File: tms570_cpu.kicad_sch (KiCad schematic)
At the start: 49 parts, among them J12 TS-103-G-A, J2 FTSH-105-01-L-DV-K, U2 TMS570LS0914PGE

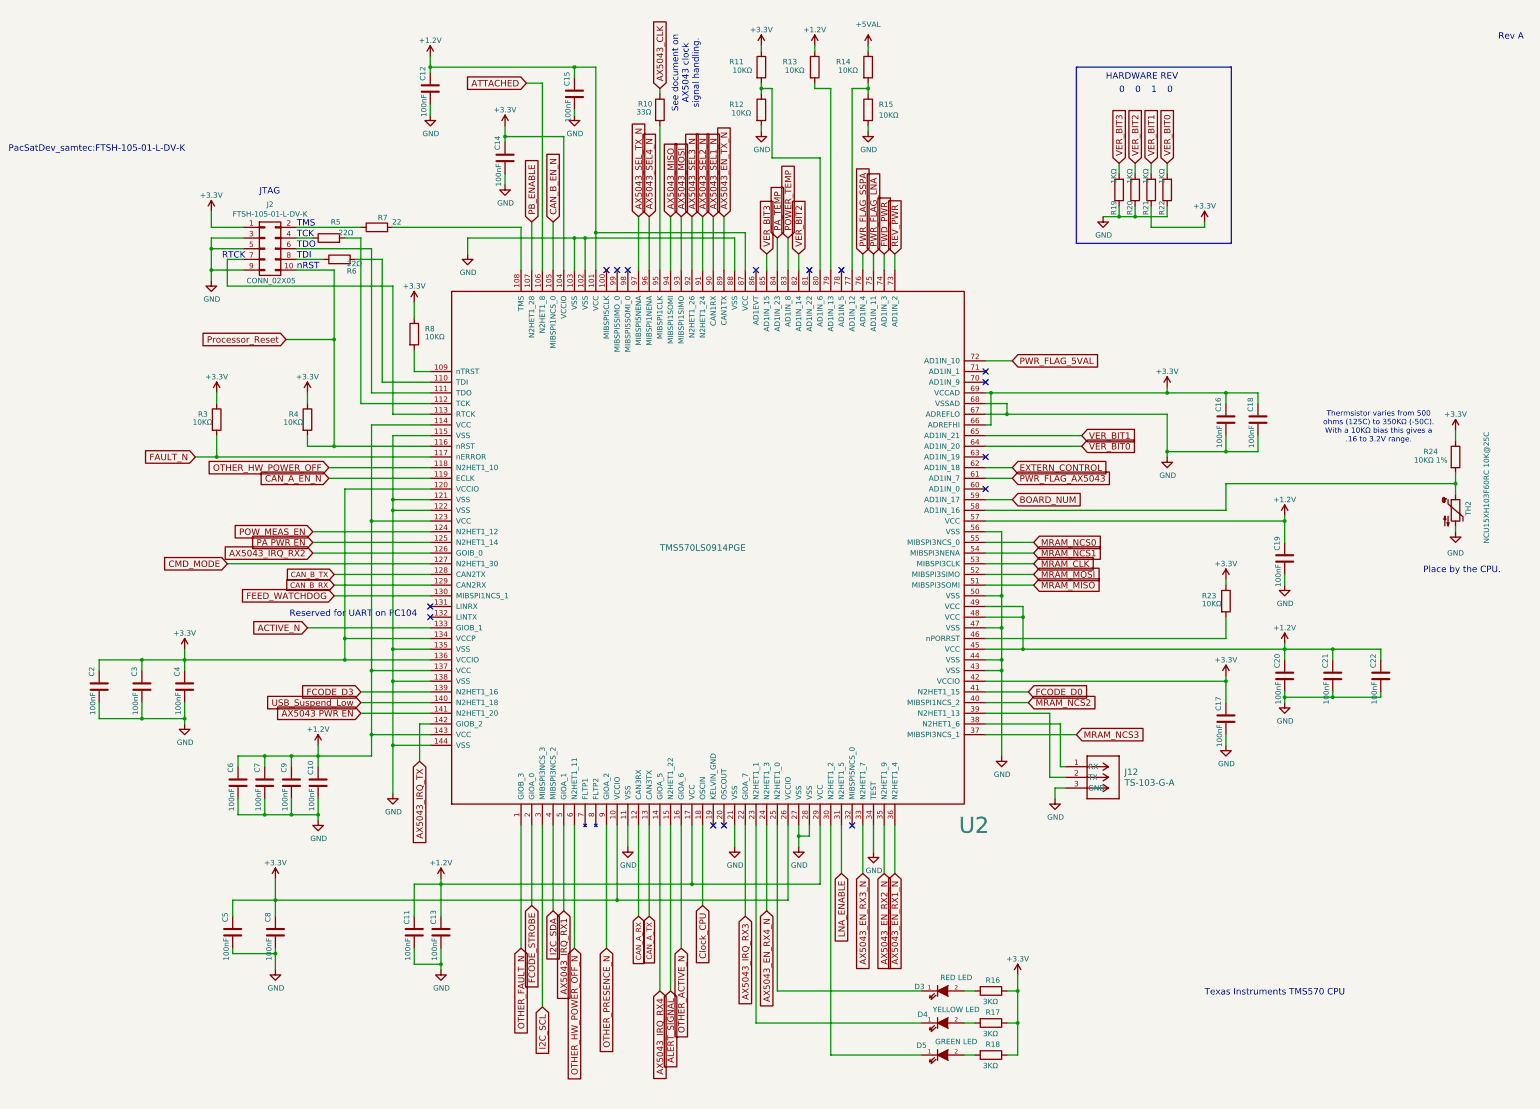
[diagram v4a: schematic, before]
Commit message: Finish up temporary PC104 assignments
Finish up most of what is required for the CubeSat Kit Bus conversion.

Signed-off-by: Corey Minyard <corey@minyard.net>
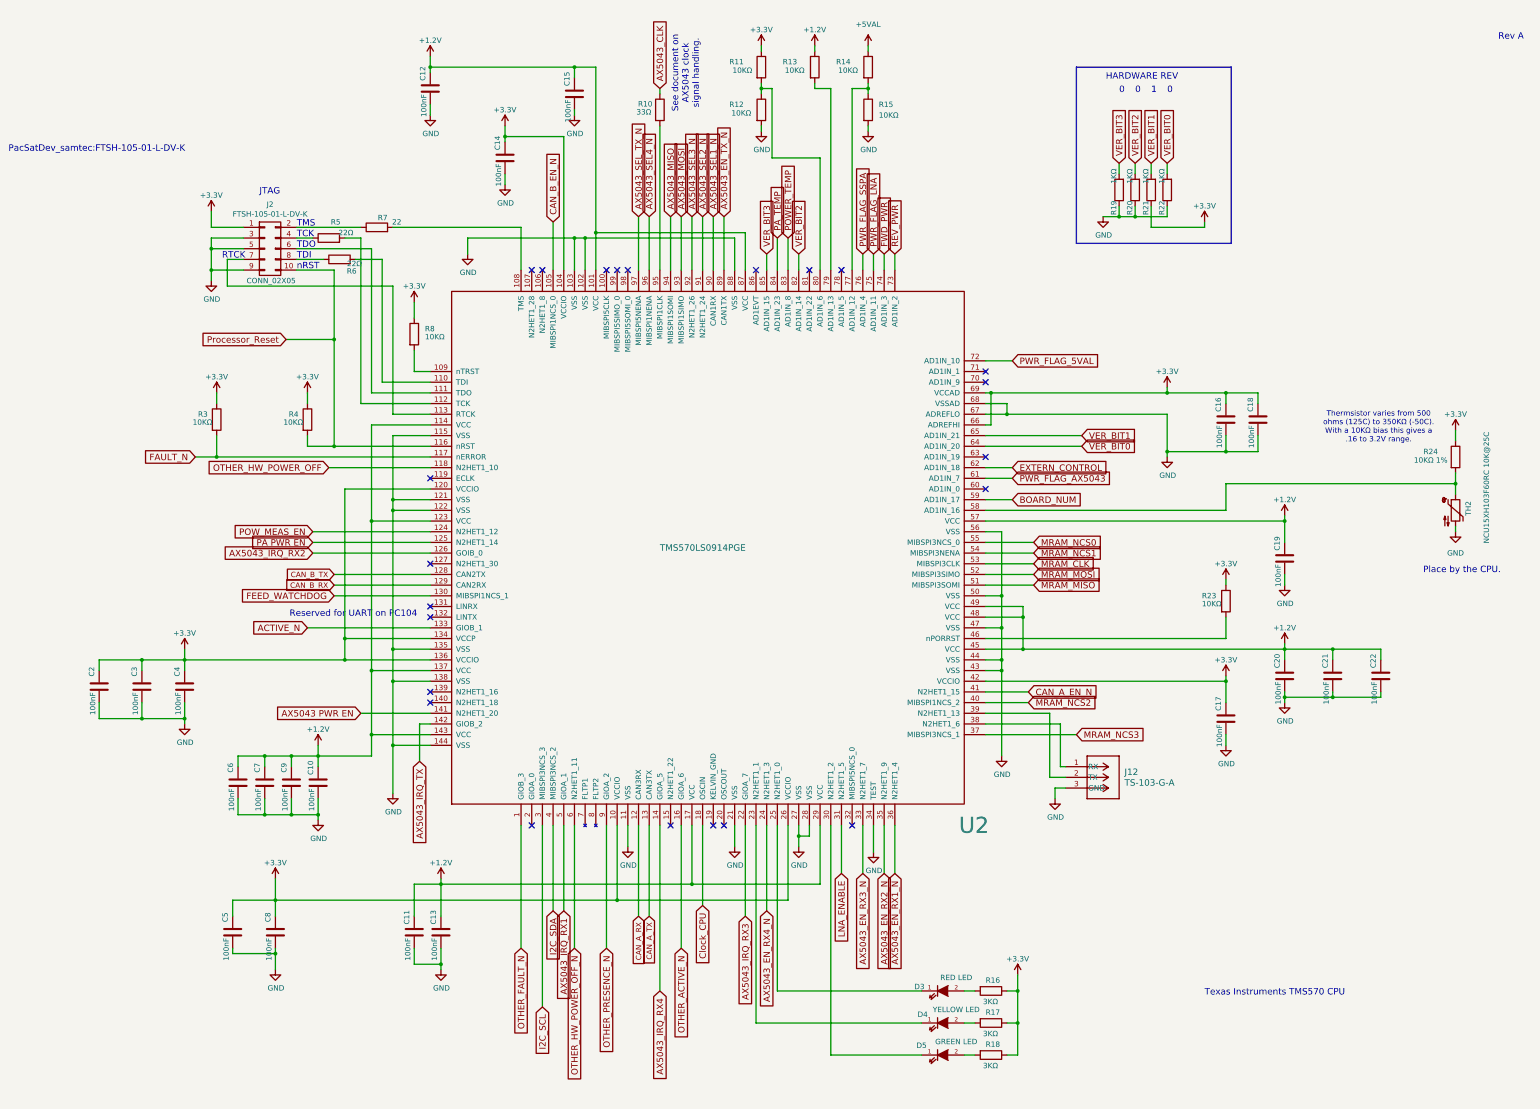
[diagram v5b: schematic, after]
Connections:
- net FCODE_D0 is gone; now on net CAN_A_EN_N: U2.41 (N2HET1_15)
- net CAN_A_EN_N: no longer U2.119 (ECLK)
- net ALERT_SIGNAL: no longer names the net of U2.15 (N2HET1_22)
- net ATTACHED: no longer names the net of U2.106 (N2HET1_8)
- net CMD_MODE: no longer names the net of U2.127 (N2HET1_30)
- net FCODE_D3: no longer names the net of U2.139 (N2HET1_16)
- net FCODE_STROBE: no longer names the net of U2.2 (GIOA_0)
- net PB_ENABLE: no longer names the net of U2.107 (N2HET1_28)
- net USB_Suspend_Low: no longer names the net of U2.140 (N2HET1_18)
- no-connect marks 15 -> 23

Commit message: Minor fixes for BOM values
Signed-off-by: Corey Minyard <corey@minyard.net>
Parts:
- R7: value 22 -> 22Ω
- TH2: value NCU15XH103F60RC 10K@25C -> NCU15XH103F60RC 10KΩ@25C
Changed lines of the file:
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@@
 			)
 		)
-		(property "Value" "NCU15XH103F60RC 10K@25C"
+		(property "Value" "NCU15XH103F60RC 10KΩ@25C"
 			(at 401.066 137.414 90)
 			(effects
@@
 			)
 		)
-		(property "Value" "22"
-			(at 143.002 60.96 90)
+		(property "Value" "22Ω"
+			(at 144.272 60.96 90)
 			(effects
 				(font
@@
 		(dnp no)
 		(property "Reference" "R5"
-			(at 128.524 60.96 90)
+			(at 131.064 66.04 90)
 			(effects
 				(font
@@
 		)
 		(property "Value" "22Ω"
-			(at 131.572 63.5 90)
+			(at 132.588 63.5 90)
 			(effects
 				(font
@@
 		(dnp no)
 		(property "Reference" "R6"
-			(at 132.334 72.644 90)
+			(at 131.318 74.168 90)
 			(effects
 				(font
@@
 		)
 		(property "Value" "22Ω"
-			(at 133.604 70.866 90)
-			(effects
-				(font
+			(at 132.588 72.39 90)
+			(effects
+				(font

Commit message: Add an UMBILICAL_ATTACHED signal from the PC104
Allow the board to know if it is in the launch vehicle.  Will
hardware inhibit transmit.

Signed-off-by: Corey Minyard <corey@minyard.net>
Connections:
- net UMBILICAL_ATTACHED: now reaches U2.119 (ECLK)
- net PA PWR EN renamed PA_PWR_EN_N
- no-connect marks 23 -> 22
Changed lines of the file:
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@@
 	)
 	(no_connect
-		(at 149.86 121.92)
-	)
-	(no_connect
 		(at 219.71 204.47)
 	)
@@
 	(wire
 		(pts
+			(xy 125.73 121.92) (xy 149.86 121.92)
+		)
+		(stroke
+			(width 0)
+			(type default)
+		)
+	)
+	(wire
+		(pts
 			(xy 232.41 204.47) (xy 232.41 243.84)
 		)
@@
 		)
 	)
+	(global_label "UMBILICAL_ATTACHED"
+		(shape input)
+		(at 125.73 121.92 180)
+		(fields_autoplaced yes)
+		(effects
+			(font
+				(size 1.524 1.524)
+			)
+			(justify right)
+		)
+		(property "Intersheetrefs" "${INTERSHEET_REFS}"
+			(at 99.2024 121.92 0)
+			(effects
+				(font
+					(size 1.27 1.27)
+				)
+				(justify right)
+				(hide yes)
+			)
+		)
+	)
 	(global_label "VER_BIT1"
 		(shape input)
@@
 		)
 	)
-	(global_label "PA PWR EN"
+	(global_label "PA_PWR_EN_N"
 		(shape input)
 		(at 121.92 137.16 180)

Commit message: A bunch of work on component selections
And little fixups for things I found.

Signed-off-by: Corey Minyard <corey@minyard.net>
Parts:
- TH2: value NCU15XH103F60RC 10KΩ@25C -> NTCG103JF103FTDS 10KΩ@25C
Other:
- note added: "Thermsistor varies from 534 ohms (125C) to 188.5KΩ (-40C). With a 10KΩ bias this gives a .17 to 3.13V range."
- note removed: "Thermsistor varies from 500 ohms (125C) to 350KΩ (-50C). With a 10KΩ bias this gives a .16 to 3.2V range."
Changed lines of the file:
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@@
 		)
 	)
-	(text "Thermsistor varies from 500\nohms (125C) to 350KΩ (-50C).\nWith a 10KΩ bias this gives a\n.16 to 3.2V range."
+	(text "Thermsistor varies from 534\nohms (125C) to 188.5KΩ (-40C).\nWith a 10KΩ bias this gives a\n.17 to 3.13V range."
 		(exclude_from_sim no)
 		(at 375.412 109.728 0)
@@
 			)
 		)
-		(property "Value" "NCU15XH103F60RC 10KΩ@25C"
+		(property "Value" "NTCG103JF103FTDS 10KΩ@25C"
 			(at 401.066 137.414 90)
 			(effects
